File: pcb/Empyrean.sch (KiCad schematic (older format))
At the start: 45 parts, among them J1 FCI 10118194-0001LF, J2 Harwin M50-3500542, J3 SPI, J4 CONN_01X15, J5 CONN_01X15, Q1 DMG1012UW-7, Q2 DMG1013T-7, Q3 DMG1013T-7, Q4 DMG1012UW-7, U1 LP2985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

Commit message: Update schematic to Rev B
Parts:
- added JP1: VUSB Disable, EtherkitKicadLibrary:SOLDER_JUMPER_NC, symbol EtherkitKicadLibrary:JUMPER-NC
- C1, C10, C11, C12, C2, C3, C4, C5, C6, C7, C8, C9: symbol C -> Empyrean-rescue:C
- D1, D2, D3, D4: symbol LED -> Empyrean-rescue:LED
- F1: symbol FUSE -> Empyrean-rescue:FUSE
- J1: symbol USB_OTG -> Empyrean-rescue:USB_OTG
- J2: symbol CONN_02X05 -> Empyrean-rescue:CONN_02X05
- J3: symbol CONN_01X03 -> Empyrean-rescue:CONN_01X03
- J4, J5: symbol CONN_01X15 -> Empyrean-rescue:CONN_01X15
- JP2: renamed from JP1; footprint EtherkitKicadLibrary:SOLDER_JUMPER -> EtherkitKicadLibrary:SOLDER_JUMPER_NC; symbol JUMPER -> EtherkitKicadLibrary:JUMPER-NC
- L1: symbol L -> Empyrean-rescue:L
- Q1, Q4: value DMG1012UW-7 -> DMG1012T-7; symbol MOS_N -> Empyrean-rescue:MOS_N
- Q2, Q3: symbol MOS_P -> Empyrean-rescue:MOS_P
- R1, R10, R11, R2, R3, R4, R5, R6, R7, R8, R9: symbol R -> Empyrean-rescue:R
- S1: symbol PUSHBUTTON -> Empyrean-rescue:PUSHBUTTON
- U1: symbol LP2985 -> Empyrean-rescue:LP2985
- U2: symbol ATSAMD21G18A -> Empyrean-rescue:ATSAMD21G18A
- VR1, VR2: symbol VR -> Empyrean-rescue:VR
- X1: symbol CRYSTAL -> Empyrean-rescue:CRYSTAL
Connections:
- net RESET: no longer J4.3 (P3)
- net at F1.1: now also JP1.2; no longer J1.1 (VCC)
- new net VUSB: J1.1 (VCC), J4.3 (P3), JP1.1
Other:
- moved on the sheet: F1

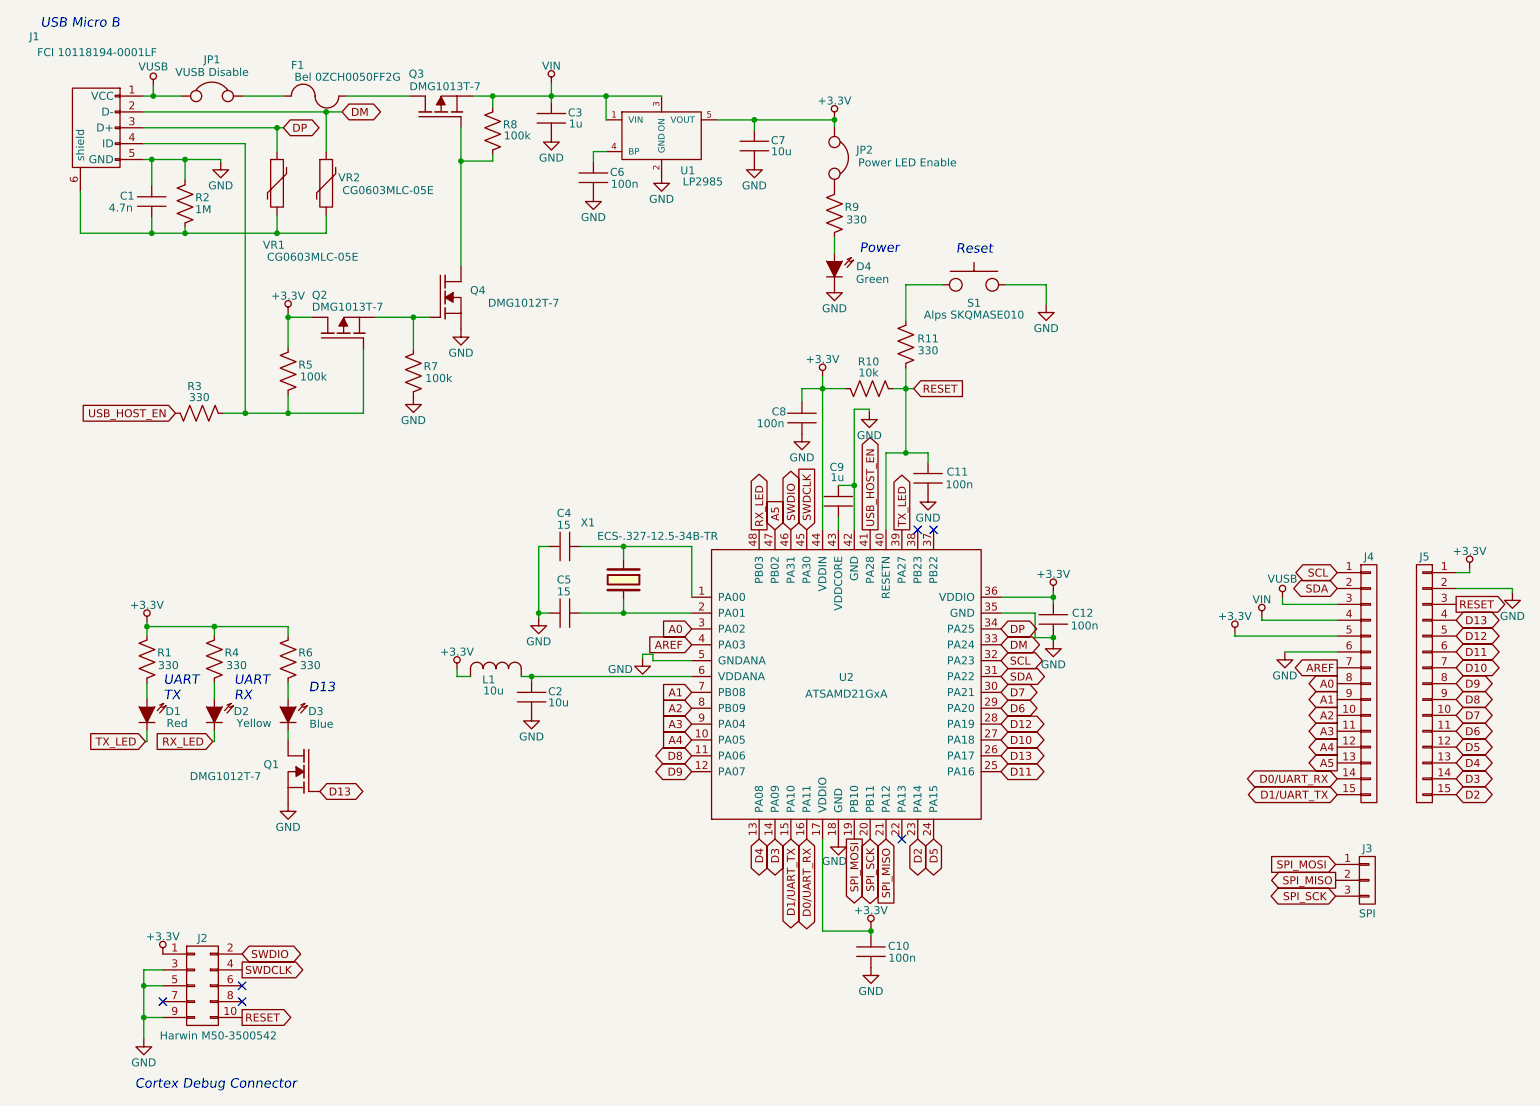
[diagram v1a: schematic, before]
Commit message: Updated PCB with castellation
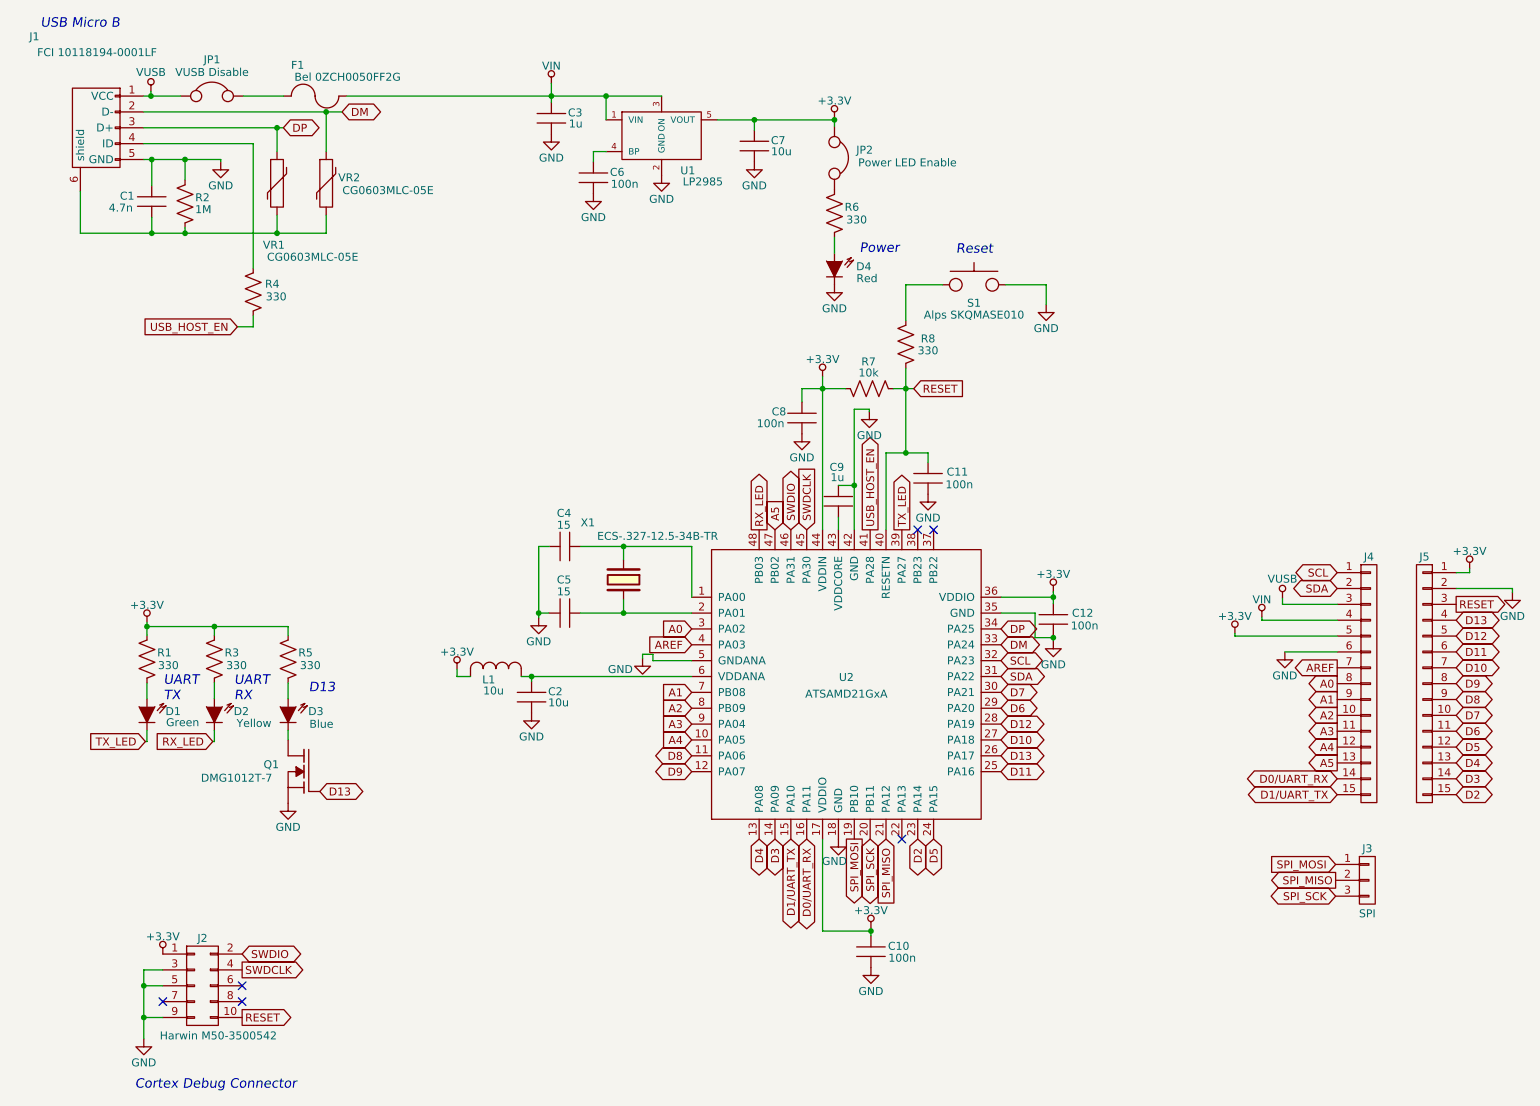
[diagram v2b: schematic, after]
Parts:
- removed Q2, Q3: DMG1013T-7, EtherkitKicadLibrary:SOT523, symbol Empyrean-rescue:MOS_P
- removed Q4: DMG1012T-7, EtherkitKicadLibrary:SOT523, symbol Empyrean-rescue:MOS_N
- removed R5, R7, R8: 100k, Resistors_SMD:R_0603, symbol Empyrean-rescue:R
- D1: value Red -> Green
- D4: value Green -> Red
- renumbered R4 to R3, R3 to R4, R6 to R5, R9 to R6, R10 to R7, R11 to R8
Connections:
- net USB_HOST_EN: now also R4.1; no longer R4.2
- net VIN: now also F1.2
- net at J1.4 (ID): now also R4.2; no longer R4.1
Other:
- moved on the sheet: R4
